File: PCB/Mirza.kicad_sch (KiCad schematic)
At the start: 99 parts, among them J1 In, J2 Out, J3 Power, Q1 BCM857DS, Q13 2SC3324, Q14 2SA1312, Q15 2SA1312, Q16 2SA1312, Q17 2SC3324, Q18 2SC3324, Q2 BCM847DS, Q21 2SA1312, Q22 2SC3324, Q23 2SC3324, Q24 2SA1312, Q25 D45H11, Q26 D44H11, Q3 2SA1312, Q4 2SC3324, Q5 2SC3324, Q6 2SC3324, Q7 2SA1312, Q8 2SA1312, U1 ADA4522-1

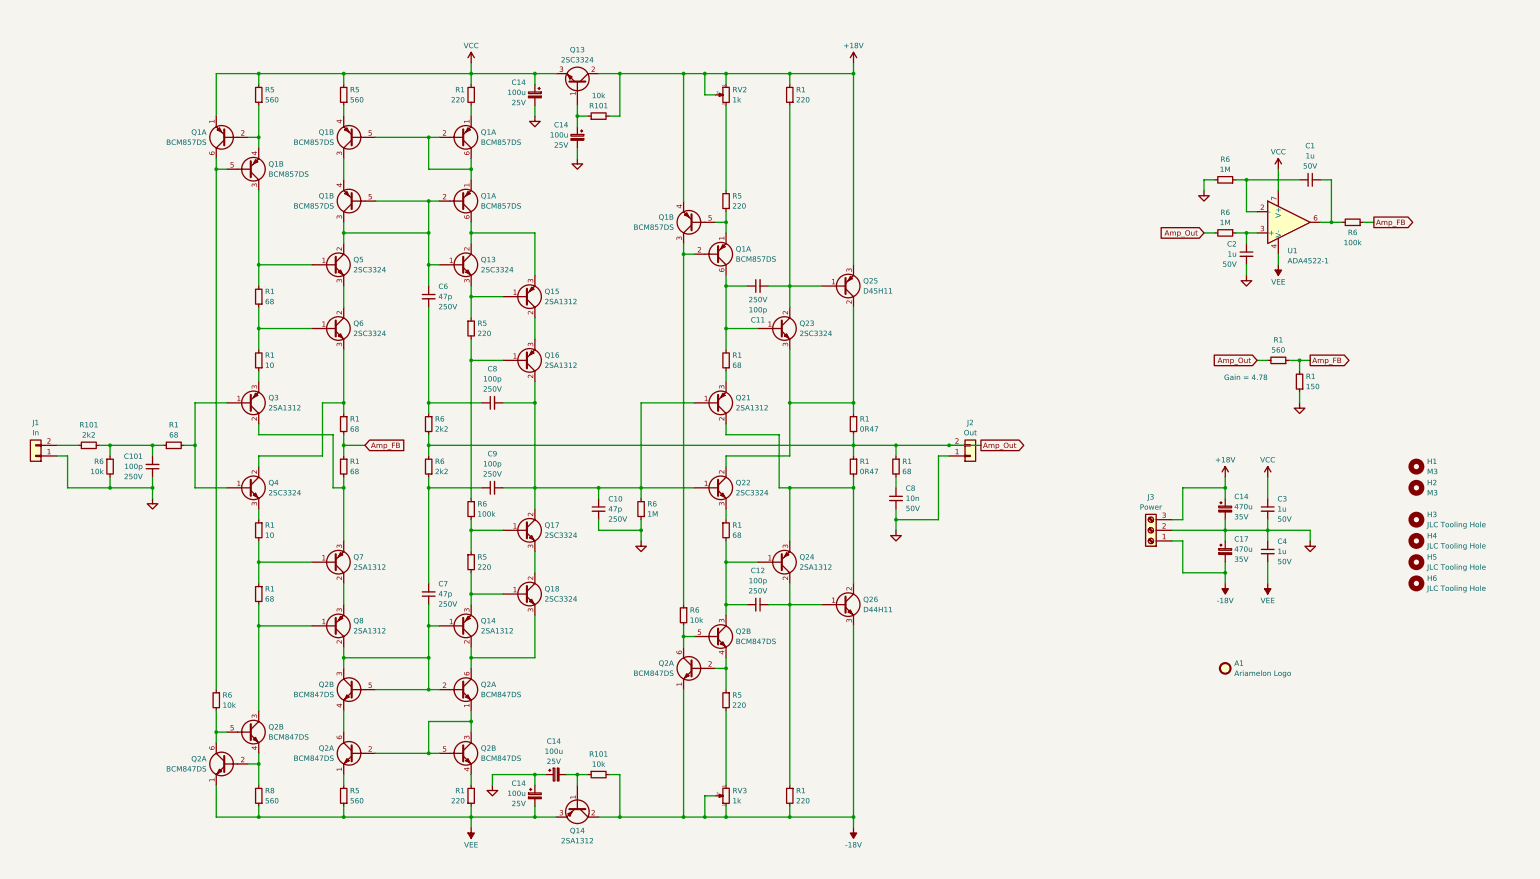
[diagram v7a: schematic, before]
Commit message: 28/09/2023 update
Changed size of emitter resistors to MELF0207 for better heat dissipation.
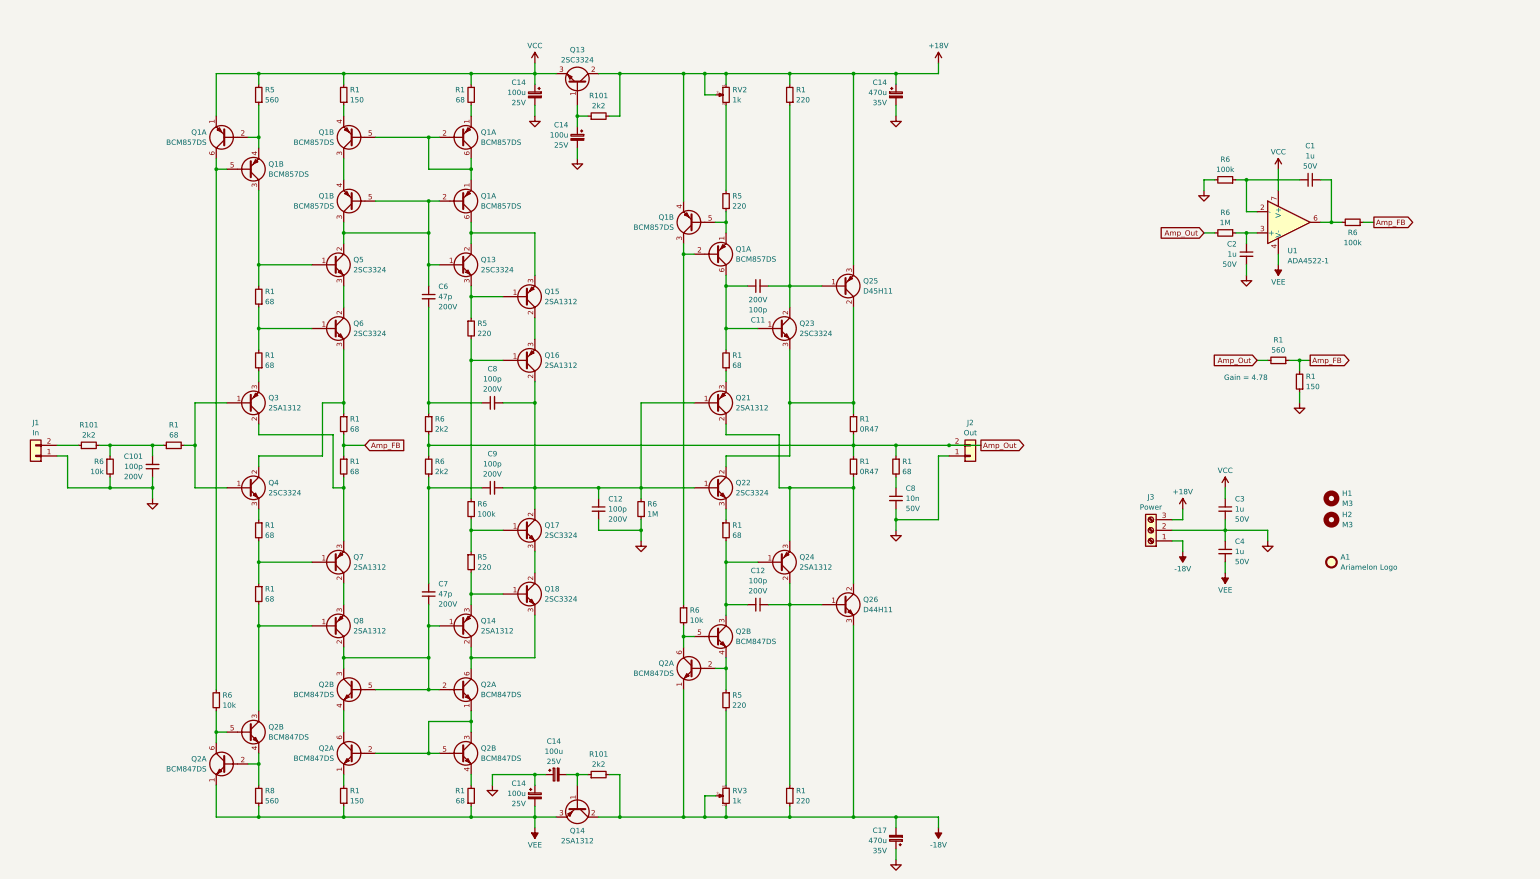
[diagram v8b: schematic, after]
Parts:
- removed C10: 47p, Ariamelon-Device:C_0805_2012Metric, symbol Device:C_Small
- removed H3, H4, H5, H6: JLC Tooling Hole, Ariamelon-HolePad:MountingHole_JLC-Tooling, symbol Mechanical:MountingHole
- removed R1 (x2): 10, Resistor_SMD:R_MiniMELF_MMA-0204, symbol Device:R_Small
- removed R1 (x2): 220, Resistor_SMD:R_MiniMELF_MMA-0204, symbol Device:R_Small
- removed R101 (x2): 10k, Resistor_SMD:R_MiniMELF_MMA-0204, symbol Device:R_Small
- removed R5 (x2): 560, Resistor_SMD:R_MiniMELF_MMA-0204, symbol Device:R_Small
- added C12: 100p, Ariamelon-Device:C_0805_2012Metric, symbol Device:C_Small
- added R1 (x4): 68, Resistor_SMD:R_MiniMELF_MMA-0204, symbol Device:R_Small
- added R1 (x2): 150, Resistor_SMD:R_MiniMELF_MMA-0204, symbol Device:R_Small
- added R101 (x2): 2k2, Resistor_SMD:R_MiniMELF_MMA-0204, symbol Device:R_Small
- C101, C11, C12, C8, C9: LCSC C437488 -> C710961; Manufacturer No. GCM21A7U2E101JX01D -> GRM21A5C2D101JW01D; Voltage 250V -> 200V
- C6, C7: LCSC C440149 -> C162302; Manufacturer No. GCM21A5C2E470JX01D -> GRM21A5C2D470JW01D; Voltage 250V -> 200V
- Q1: LCSC (none) -> C549564; Voltage C549564 -> (none)
- Q2: LCSC (none) -> C549558; Voltage C549558 -> (none)
- R1: footprint Resistor_SMD:R_MiniMELF_MMA-0204 -> Resistor_SMD:R_MELF_MMB-0207; LCSC C2089943 -> C2079987; Manufacturer No. MMA02040C4707FB300 -> MMB02070C4707FB200
- R6: value 1M -> 100k; LCSC C4339242 -> C2836210; Manufacturer No. MMA02040C1004FB300 -> MMA02040C1003FB300
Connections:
- net +18V: now also R101.2
- net -18V: now also R101.2
- net Amp_Out: now also R1.2; no longer R1.1
- net GND: now also C12.2
- net VCC: now also R1.1, R1.2
- net VEE: now also R1.1, R1.1
- net at Q3.3 (E): now also R1.1
- net at Q6.1 (B), R1.1: now also R1.2
- net at Q21.2 (C), Q24.3 (E), Q26.2 (C): now also R1.1; no longer R1.2
- net at C8.2, C9.2, Q16.2 (C)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: now also C12.1
- net at C14.2, Q14.1 (B): now also R101.1
- net at C14.1, Q13.1 (B): now also R101.1
- net at Q2.4 (E2): now also R1.2
- net at Q2.1 (E1): now also R1.2
- net at Q7.1 (B), R1.1: now also R1.2
- net at Q4.3 (E): now also R1.1
- net at Q1.1 (E1): now also R1.2
- net at Q1.4 (E2): now also R1.1
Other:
- moved on the sheet: A1, C14, C17, C3, C4, H1, H2, R1
